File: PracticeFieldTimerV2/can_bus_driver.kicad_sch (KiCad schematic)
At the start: 5 parts, among them J8 CAN Terminate, U5 SN65HVD230DR

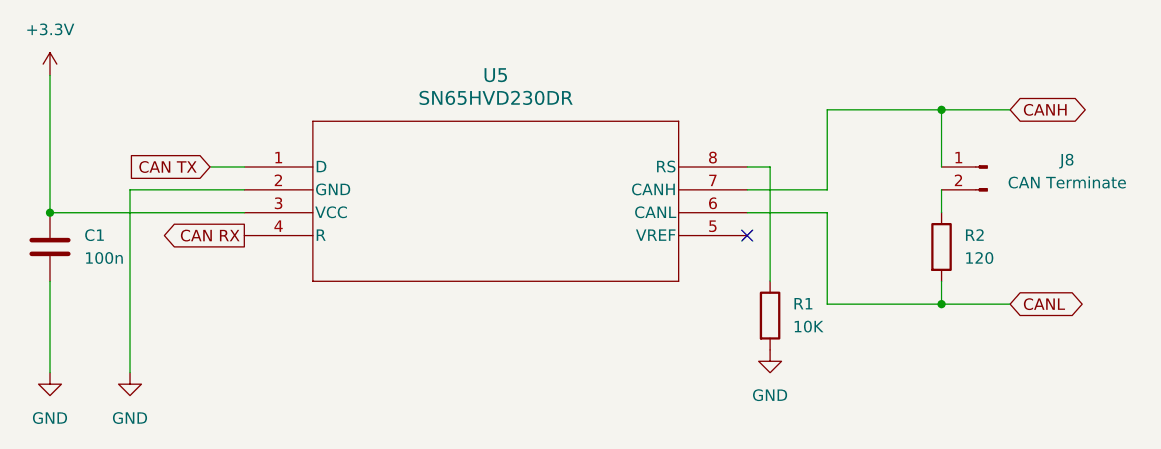
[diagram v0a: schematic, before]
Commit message: More cleanup: redraw the cut lines to precise dimensions, minor improvements to symbol appearance.
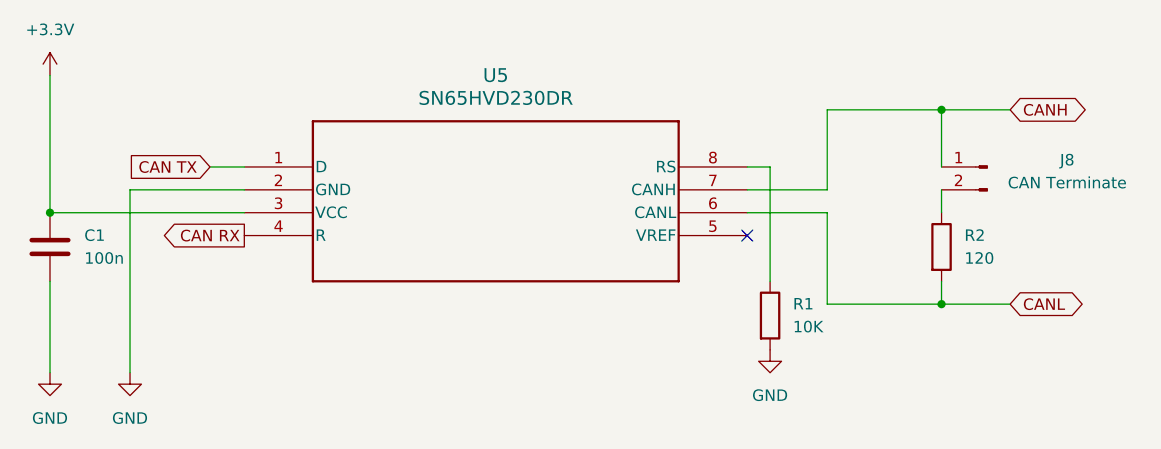
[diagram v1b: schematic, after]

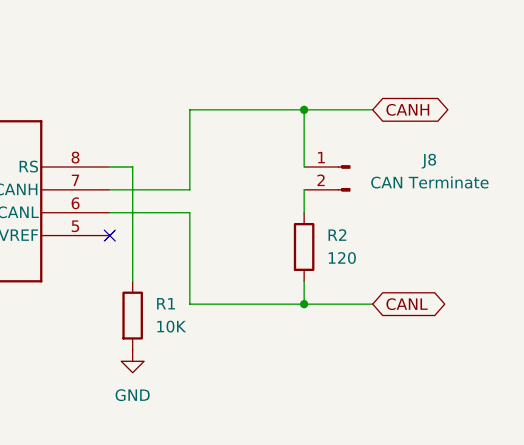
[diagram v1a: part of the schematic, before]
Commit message: Remove on-board LCD Module and I2C->parallel byte converter. Add terminal strip for off-board display. Shrink the board. The board is still a bit spread out, but the changes are significant enough to commit.
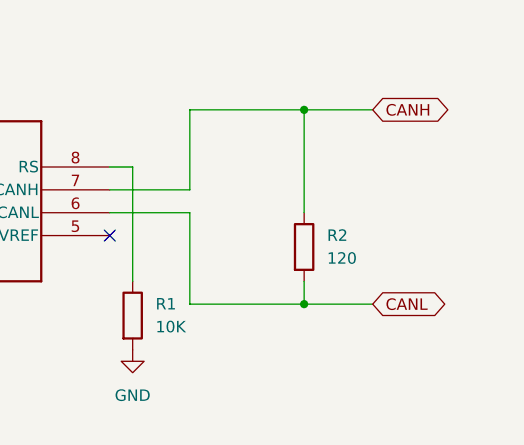
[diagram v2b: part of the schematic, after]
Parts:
- removed J8: CAN Terminate, Connector_PinHeader_2.54mm:PinHeader_1x02_P2.54mm_Vertical, symbol Connector:Conn_01x02_Pin
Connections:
- net CANH: now also R2.1
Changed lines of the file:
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@@
 	(wire
 		(pts
-			(xy 173.99 95.25) (xy 173.99 97.79)
-		)
-		(stroke
-			(width 0)
-			(type default)
-		)
-	)
-	(wire
-		(pts
-			(xy 173.99 86.36) (xy 173.99 92.71)
+			(xy 173.99 86.36) (xy 173.99 97.79)
 		)
 		(stroke
@@
 					(unit 1)
 				)
-			)
-		)
-	)
-	(symbol
-		(lib_id "Connector:Conn_01x02_Pin")
-		(at 179.07 92.71 0)
-		(mirror y)
-		(unit 1)
-		(exclude_from_sim no)
-		(in_bom yes)
-		(on_board yes)
-		(dnp no)
-		(property "Reference" "J8"
-			(at 187.96 91.948 0)
-			(effects
-				(font
-					(size 1.27 1.27)
-				)
-			)
-		)
-		(property "Value" "CAN Terminate"
-			(at 187.96 94.488 0)
-			(effects
-				(font
-					(size 1.27 1.27)
-				)
-			)
-		)
-		(property "Footprint" "Connector_PinHeader_2.54mm:PinHeader_1x02_P2.54mm_Vertical"
-			(at 179.07 92.71 0)
-			(effects
-				(font
-					(size 1.27 1.27)
-				)
-				(hide yes)
-			)
-		)
-		(property "Datasheet" "~"
-			(at 179.07 92.71 0)
-			(effects
-				(font
-					(size 1.27 1.27)
-				)
-				(hide yes)
-			)
-		)
-		(property "Description" "Generic connector, single row, 01x02, script generated"
-			(at 179.07 92.71 0)
-			(effects
-				(font
-					(size 1.27 1.27)
-				)
-				(hide yes)
-			)
-		)
-		(pin "2"
-		)
-		(pin "1"
-		)
-		(instances
-			(project "PracticeFieldTimerV2"
-				(path "/a82ebad5-0442-461b-8944-6652da9a0796/3f1a8007-b28c-46a9-9417-5626ab696631"
-					(reference "J8")
-					(unit 1)
-				)

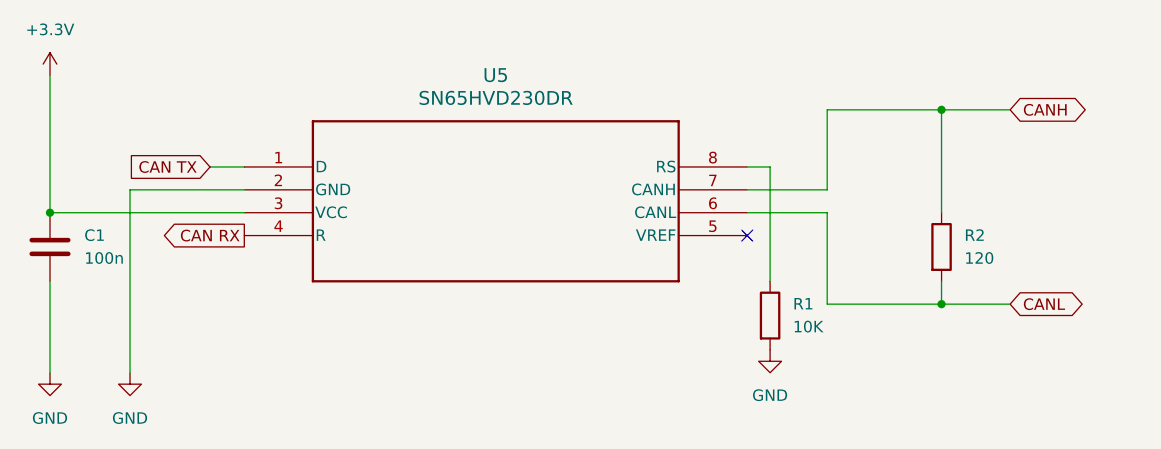
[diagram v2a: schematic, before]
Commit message: Add jumper pins to control CAN bus termination. Counters at the end of the CAN bus MUST connect the pins. Others MUST leave the pins disconnected.
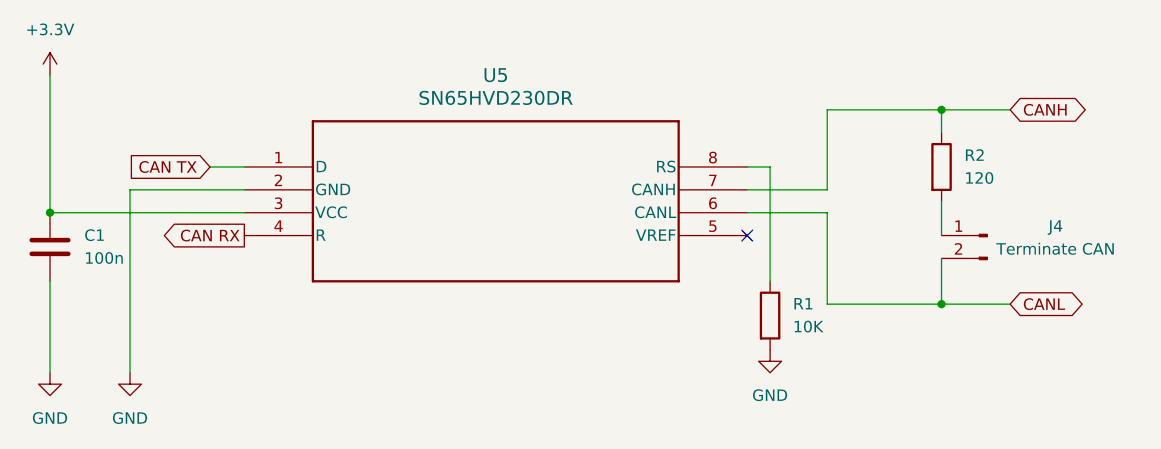
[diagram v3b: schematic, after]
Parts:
- added J4: Terminate CAN, Connector_PinHeader_2.54mm:PinHeader_1x02_P2.54mm_Vertical, symbol Connector:Conn_01x02_Pin
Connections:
- net CANL: now also J4.2 (Pin_2); no longer R2.2
- new net: J4.1 (Pin_1), R2.2
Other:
- moved on the sheet: R2
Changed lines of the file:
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@@
+	)
+	(junction
+		(at 74.93 97.79)
+		(diameter 0)
+		(color 0 0 0 0)
 	)
 	(junction
@@
 	)
 	(junction
-		(at 74.93 97.79)
-		(diameter 0)
-		(color 0 0 0 0)
-	)
-	(junction
 		(at 173.99 86.36)
 		(diameter 0)
@@
 	(wire
 		(pts
+			(xy 173.99 102.87) (xy 173.99 107.95)
+		)
+		(stroke
+			(width 0)
+			(type default)
+		)
+	)
+	(wire
+		(pts
 			(xy 161.29 97.79) (xy 161.29 107.95)
 		)
@@
 	(wire
 		(pts
-			(xy 173.99 105.41) (xy 173.99 107.95)
+			(xy 173.99 96.52) (xy 173.99 100.33)
 		)
 		(stroke
@@
 	(wire
 		(pts
+			(xy 74.93 105.41) (xy 74.93 115.57)
+		)
+		(stroke
+			(width 0)
+			(type default)
+		)
+	)
+	(wire
+		(pts
+			(xy 173.99 86.36) (xy 181.61 86.36)
+		)
+		(stroke
+			(width 0)
+			(type default)
+		)
+	)
+	(wire
+		(pts
+			(xy 152.4 95.25) (xy 161.29 95.25)
+		)
+		(stroke
+			(width 0)
+			(type default)
+		)
+	)
+	(wire
+		(pts
+			(xy 173.99 86.36) (xy 173.99 88.9)
+		)
+		(stroke
+			(width 0)
+			(type default)
+		)
+	)
+	(wire
+		(pts
+			(xy 74.93 97.79) (xy 74.93 82.55)
+		)
+		(stroke
+			(width 0)
+			(type default)
+		)
+	)
+	(wire
+		(pts
+			(xy 161.29 86.36) (xy 173.99 86.36)
+		)
+		(stroke
+			(width 0)
+			(type default)
+		)
+	)
+	(wire
+		(pts
+			(xy 92.71 92.71) (xy 96.52 92.71)
+		)
+		(stroke
+			(width 0)
+			(type default)
+		)
+	)
+	(wire
+		(pts
 			(xy 173.99 107.95) (xy 181.61 107.95)
-		)
-		(stroke
-			(width 0)
-			(type default)
-		)
-	)
-	(wire
-		(pts
-			(xy 74.93 105.41) (xy 74.93 115.57)
-		)
-		(stroke
-			(width 0)
-			(type default)
-		)
-	)
-	(wire
-		(pts
-			(xy 173.99 86.36) (xy 181.61 86.36)
-		)
-		(stroke
-			(width 0)
-			(type default)
-		)
-	)
-	(wire
-		(pts
-			(xy 152.4 95.25) (xy 161.29 95.25)
-		)
-		(stroke
-			(width 0)
-			(type default)
-		)
-	)
-	(wire
-		(pts
-			(xy 173.99 86.36) (xy 173.99 97.79)
-		)
-		(stroke
-			(width 0)
-			(type default)
-		)
-	)
-	(wire
-		(pts
-			(xy 74.93 97.79) (xy 74.93 82.55)
-		)
-		(stroke
-			(width 0)
-			(type default)
-		)
-	)
-	(wire
-		(pts
-			(xy 161.29 86.36) (xy 173.99 86.36)
-		)
-		(stroke
-			(width 0)
-			(type default)
-		)
-	)
-	(wire
-		(pts
-			(xy 92.71 92.71) (xy 96.52 92.71)
 		)
 		(stroke
@@
 	(symbol
 		(lib_id "Device:R")
-		(at 173.99 101.6 0)
+		(at 173.99 92.71 0)
 		(unit 1)
 		(exclude_from_sim no)
@@
 		(fields_autoplaced yes)
 		(property "Reference" "R2"
-			(at 176.53 100.3299 0)
+			(at 176.53 91.4399 0)
 			(effects
 				(font
@@
 		)
 		(property "Value" "120"
-			(at 176.53 102.8699 0)
+			(at 176.53 93.9799 0)
 			(effects
 				(font
@@
 		)
 		(property "Footprint" "Resistor_THT:R_Axial_DIN0207_L6.3mm_D2.5mm_P15.24mm_Horizontal"
-			(at 172.212 101.6 90)
+			(at 172.212 92.71 90)
 			(effects
 				(font
@@
 		)
 		(property "Datasheet" "~"
-			(at 173.99 101.6 0)
+			(at 173.99 92.71 0)
 			(effects
 				(font
@@
 		)
 		(property "Description" "Resistor"
-			(at 173.99 101.6 0)
+			(at 173.99 92.71 0)
 			(effects
 				(font
@@
 					(unit 1)
 				)
+			)
+		)
+	)
+	(symbol
+		(lib_id "Connector:Conn_01x02_Pin")
+		(at 179.07 100.33 0)
+		(mirror y)
+		(unit 1)
+		(exclude_from_sim no)
+		(in_bom yes)
+		(on_board yes)
+		(dnp no)
+		(property "Reference" "J4"
+			(at 186.69 99.314 0)
+			(effects
+				(font
+					(size 1.27 1.27)
+				)
+			)
+		)
+		(property "Value" "Terminate CAN"
+			(at 186.69 101.854 0)
+			(effects
+				(font
+					(size 1.27 1.27)
+				)
+			)
+		)
+		(property "Footprint" "Connector_PinHeader_2.54mm:PinHeader_1x02_P2.54mm_Vertical"
+			(at 179.07 100.33 0)
+			(effects
+				(font
+					(size 1.27 1.27)
+				)
+				(hide yes)
+			)
+		)
+		(property "Datasheet" "~"
+			(at 179.07 100.33 0)
+			(effects
+				(font
+					(size 1.27 1.27)
+				)
+				(hide yes)
+			)
+		)
+		(property "Description" "Generic connector, single row, 01x02, script generated"
+			(at 179.07 100.33 0)
+			(effects
+				(font
+					(size 1.27 1.27)
+				)
+				(hide yes)
+			)
+		)
+		(pin "2"
+		)
+		(pin "1"
+		)
+		(instances
+			(project "PracticeFieldTimerV2"
+				(path "/a82ebad5-0442-461b-8944-6652da9a0796/3f1a8007-b28c-46a9-9417-5626ab696631"
+					(reference "J4")
+					(unit 1)
+				)
